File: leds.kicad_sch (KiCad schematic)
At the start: 22 parts, among them U2 AMS1117-5.0

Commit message: before auto route
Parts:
- removed D43: WS2812B-2020, LED_SMD:LED_WS2812B_PLCC4_5.0x5.0mm_P3.2mm, symbol LED:WS2812B-2020
- added C14, C15: 1uF, Capacitor_SMD:C_0402_1005Metric, symbol Device:C
- added Q1: BSS138, Package_TO_SOT_SMD:SOT-23, symbol Transistor_FET:BSS138
- added R5, R6: 10K, Resistor_SMD:R_0201_0603Metric, symbol Device:R
- renumbered D25 to D24, D27 to D25, D29 to D26, D31 to D27, D32 to D28, D30 to D29, D28 to D30, D26 to D31, D24 to D32, D35 to D34, D37 to D35, D39 to D36, D41 to D37, D42 to D38, D40 to D39, D38 to D40, D36 to D41, D34 to D42
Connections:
- net GND: now also C14.2, C15.2
- net LED_5V: now also C15.1, R6.1
- net LED_PIN: now also Q1.2 (S), R5.2; no longer D23.3 (DIN)
- net nRF_VDDH renamed 3.2V-5V
- net 3.2V-5V: now also C14.1
- new net DATA: D23.3 (DIN), Q1.3 (D), R6.2
- new net V_SYS: Q1.1 (G), R5.1
- no-connect marks 1 -> 0
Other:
- note removed: "LEDs"
- moved on the sheet: D23, D24, D25, D26, D27, D28, D29, D30, D31, D32, D33, D34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

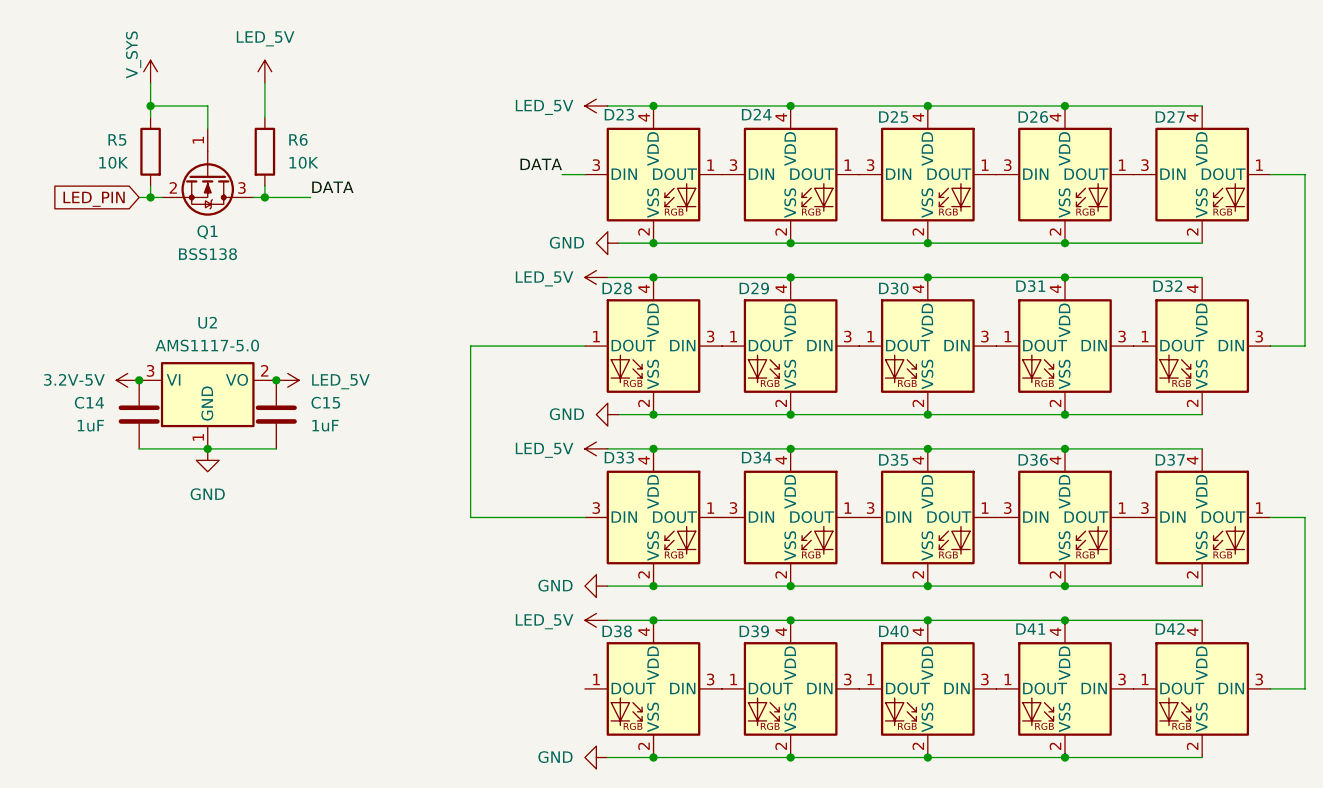
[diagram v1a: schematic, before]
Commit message: reassigned basic components, now comes the leds
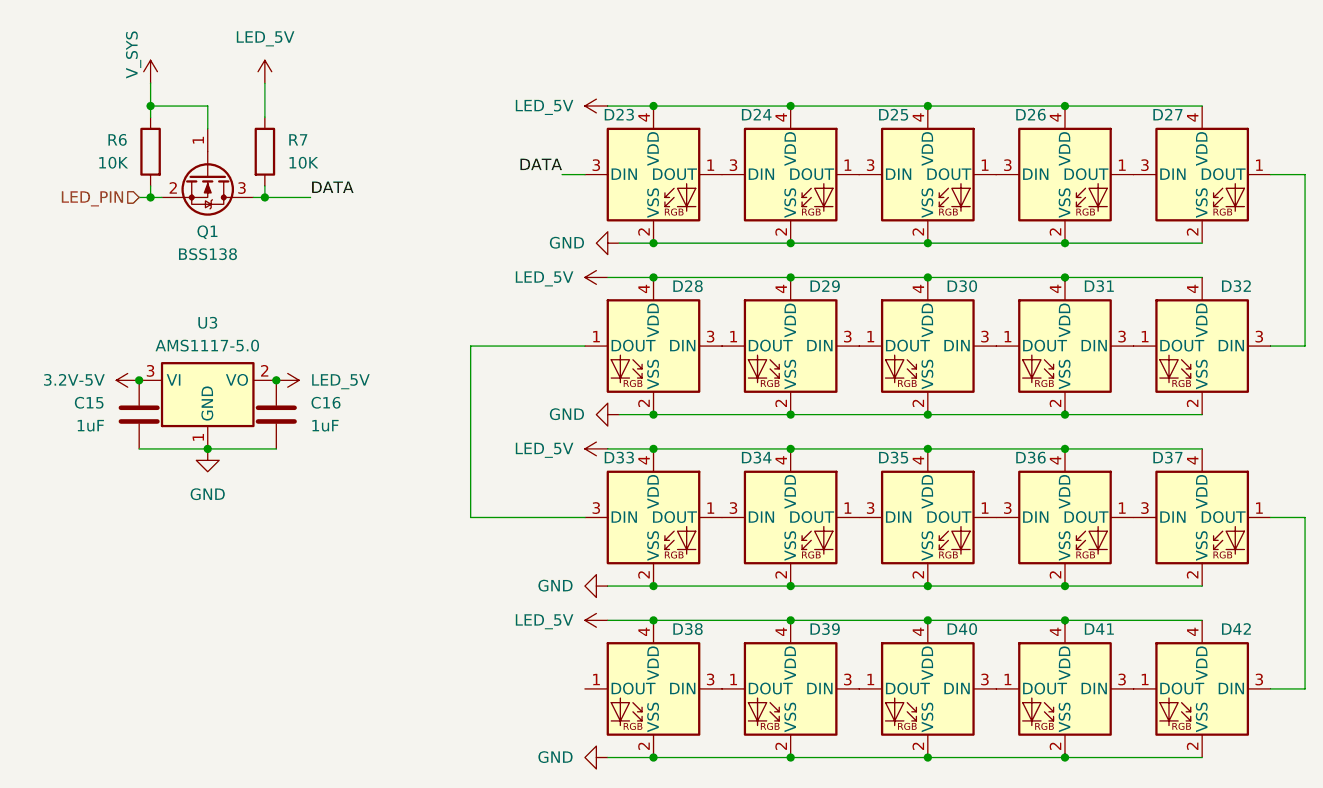
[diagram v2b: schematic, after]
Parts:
- removed D23, D24, D25, D26, D27, D28, D29, D30, D31, D32, D33, D34, D35, D36, D37, D38, D39, D40, D41, D42: WS2812B-2020, LED_SMD:LED_WS2812B_PLCC4_5.0x5.0mm_P3.2mm, symbol LED:WS2812B-2020
- added D23, D24, D25, D26, D27, D28, D29, D30, D31, D32, D33, D34, D35, D36, D37, D38, D39, D40, D41, D42: SK6812MINI, Keebio_Parts:SK6812-MINI-E, symbol LED:SK6812MINI
- renumbered C14 to C15, C15 to C16, R5 to R6, R6 to R7, U2 to U3
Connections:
- net DATA: now also D23.3 (DIN)
- net GND: now also D23.2 (VSS), D24.2 (VSS), D25.2 (VSS), D26.2 (VSS), D27.2 (VSS), D28.2 (VSS), D29.2 (VSS), D30.2 (VSS), D31.2 (VSS), D32.2 (VSS), D33.2 (VSS), D34.2 (VSS), D35.2 (VSS), D36.2 (VSS), D37.2 (VSS), D38.2 (VSS), D39.2 (VSS), D40.2 (VSS), D41.2 (VSS), D42.2 (VSS)
- net LED_5V: now also D23.4 (VDD), D24.4 (VDD), D25.4 (VDD), D26.4 (VDD), D27.4 (VDD), D28.4 (VDD), D29.4 (VDD), D30.4 (VDD), D31.4 (VDD), D32.4 (VDD), D33.4 (VDD), D34.4 (VDD), D35.4 (VDD), D36.4 (VDD), D37.4 (VDD), D38.4 (VDD), D39.4 (VDD), D40.4 (VDD), D41.4 (VDD), D42.4 (VDD)
- new net: D39.3 (DIN), D40.1 (DOUT)
- new net: D40.3 (DIN), D41.1 (DOUT)
- new net: D26.1 (DOUT), D27.3 (DIN)
- new net: D25.1 (DOUT), D26.3 (DIN)
- new net: D28.3 (DIN), D29.1 (DOUT)
- new net: D29.3 (DIN), D30.1 (DOUT)
- new net: D23.1 (DOUT), D24.3 (DIN)
- new net: D24.1 (DOUT), D25.3 (DIN)
- new net: D35.1 (DOUT), D36.3 (DIN)
- new net: D34.1 (DOUT), D35.3 (DIN)
- new net: D41.3 (DIN), D42.1 (DOUT)
- new net: D33.1 (DOUT), D34.3 (DIN)
- new net: D30.3 (DIN), D31.1 (DOUT)
- new net: D31.3 (DIN), D32.1 (DOUT)
- new net: D37.1 (DOUT), D42.3 (DIN)
- new net: D36.1 (DOUT), D37.3 (DIN)
- new net: D38.3 (DIN), D39.1 (DOUT)
- new net: D27.1 (DOUT), D32.3 (DIN)
- new net: D28.1 (DOUT), D33.3 (DIN)

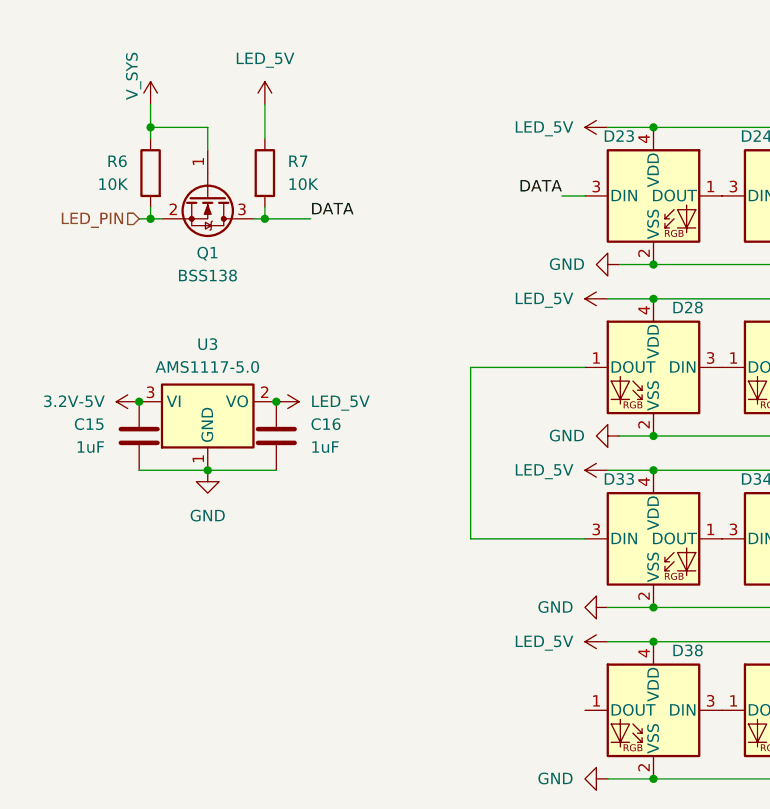
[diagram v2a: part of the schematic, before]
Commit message: placed right side
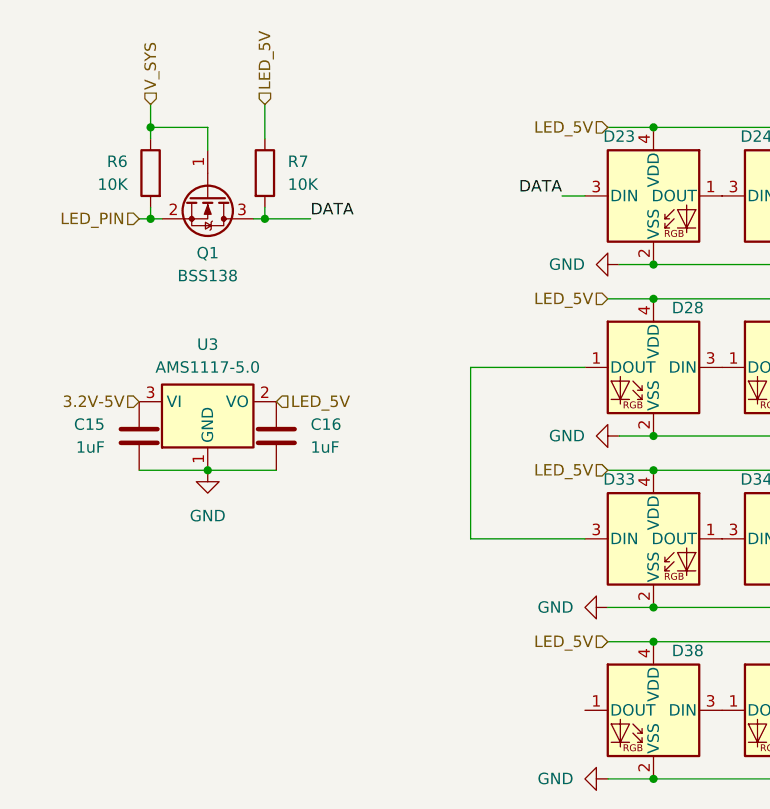
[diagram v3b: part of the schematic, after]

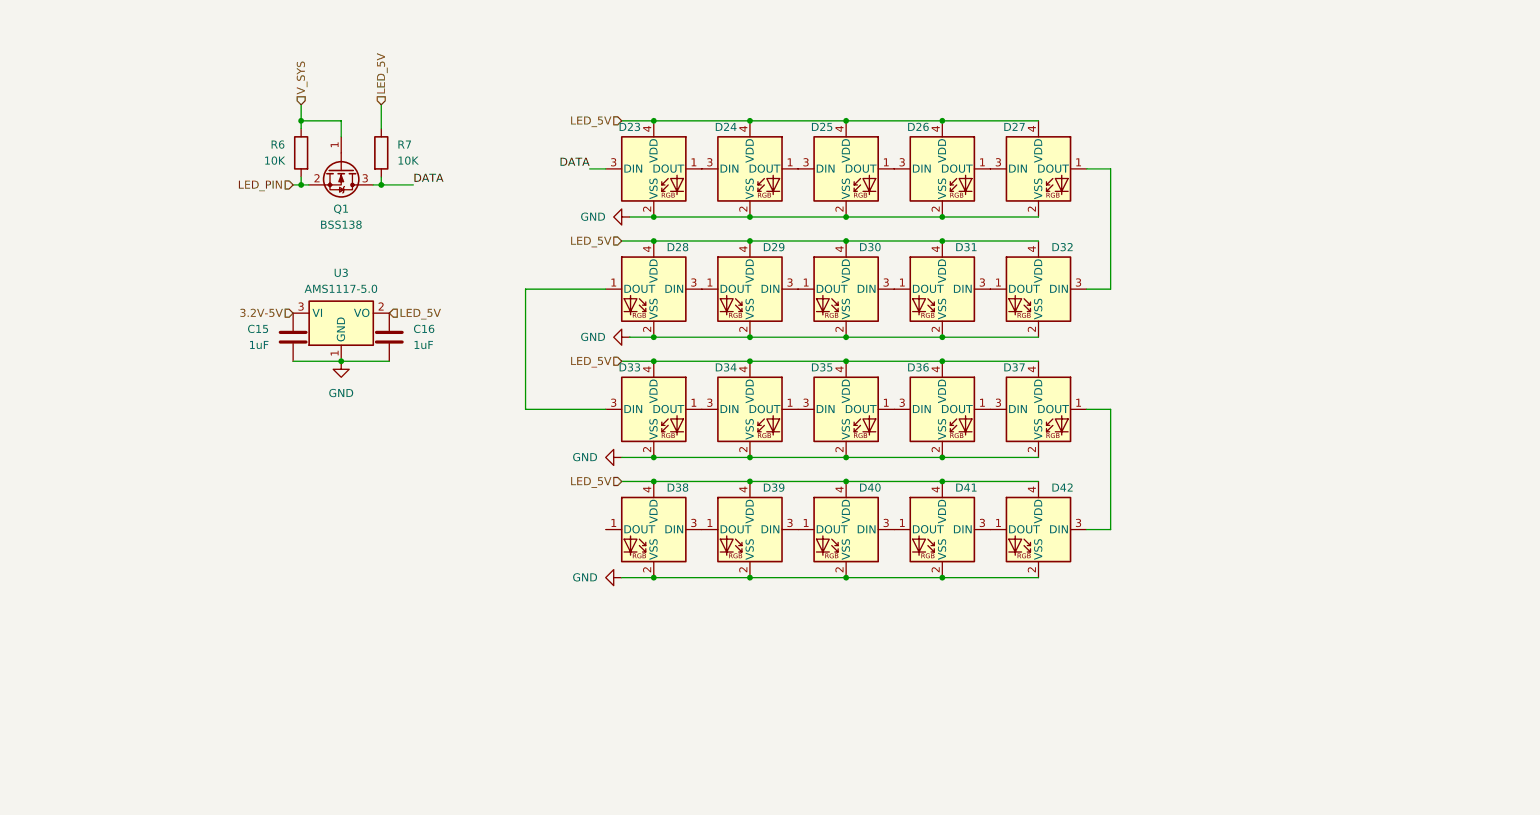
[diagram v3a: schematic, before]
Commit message: wired up the new votlage converter, removed small smd componenets
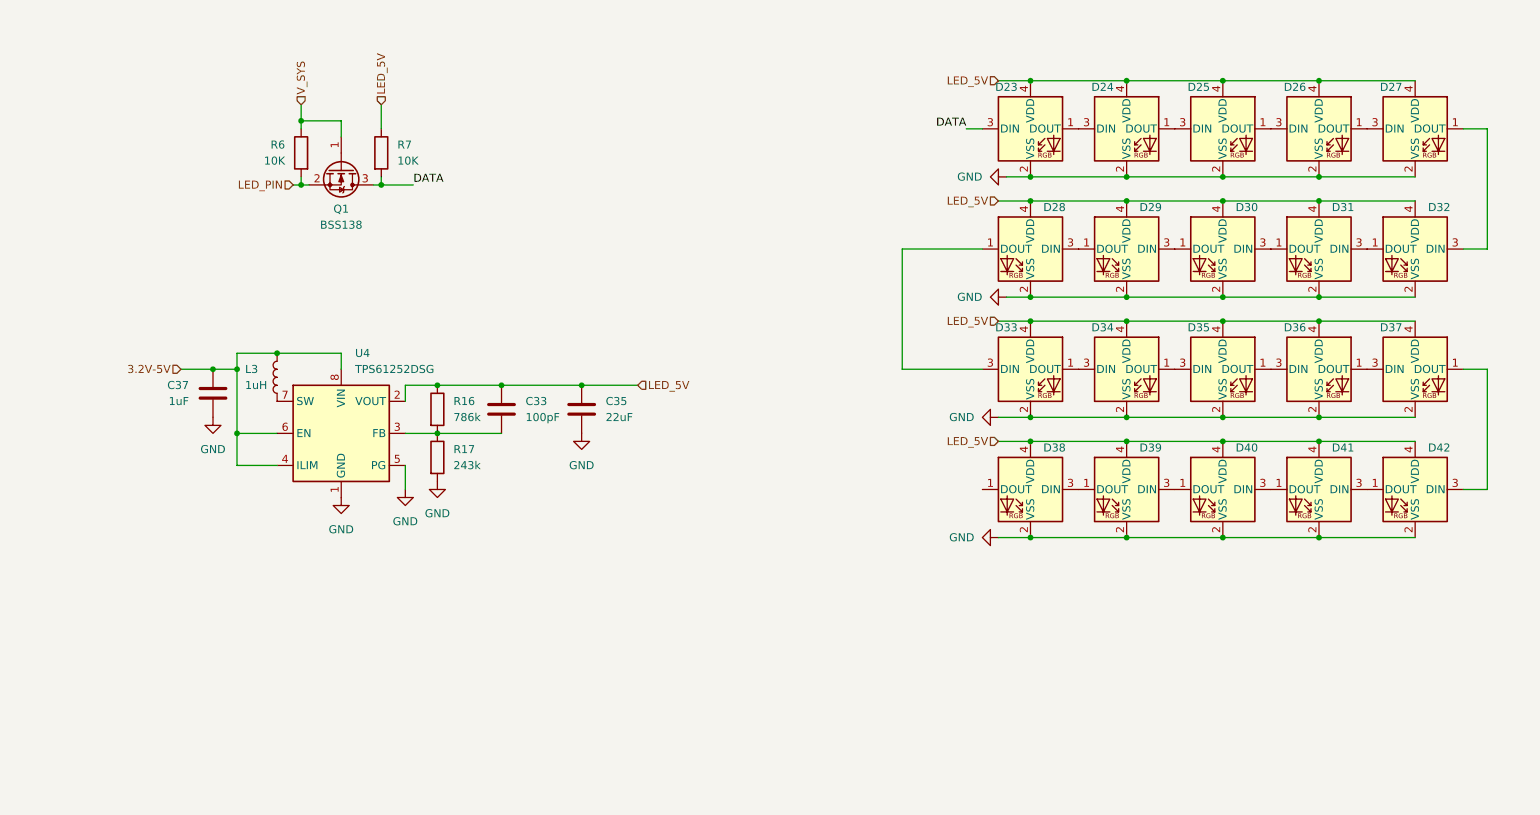
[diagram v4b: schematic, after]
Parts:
- removed C15, C16: 1uF, Capacitor_SMD:C_0402_1005Metric, symbol Device:C
- removed U3: AMS1117-5.0, Package_TO_SOT_SMD:SOT-223-3_TabPin2, symbol Regulator_Linear:AMS1117-5.0
- added C33: 100pF, Capacitor_SMD:C_0603_1608Metric, symbol Device:C
- added C35: 22uF, Capacitor_SMD:C_0603_1608Metric, symbol Device:C
- added C37: 1uF, Capacitor_SMD:C_0603_1608Metric, symbol Device:C
- added L3: 1uH, Inductor_SMD:L_0402_1005Metric, symbol Device:L
- added R16: 786k, Resistor_SMD:R_0402_1005Metric, symbol Device:R
- added R17: 243k, Resistor_SMD:R_0402_1005Metric, symbol Device:R
- added U4: TPS61252DSG, Package_SON:WSON-8-1EP_2x2mm_P0.5mm_EP0.9x1.6mm, symbol Regulator_Switching:TPS61252DSG
- R6, R7: footprint Resistor_SMD:R_0201_0603Metric -> Resistor_SMD:R_0402_1005Metric
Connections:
- net 3.2V-5V: now also C37.1, L3.2, U4.4 (ILIM), U4.6 (EN), U4.8 (VIN)
- net GND: now also C35.2, C37.2, R17.2, U4.1 (GND), U4.5 (PG), U4.9 (GND)
- net LED_5V: now also C33.1, C35.1, R16.1, U4.2 (VOUT)
- new net: C33.2, R16.2, R17.1, U4.3 (FB)
- new net: L3.1, U4.7 (SW)
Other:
- moved on the sheet: D23, D24, D25, D26, D27, D28, D29, D30, D31, D32, D33, D34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

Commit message: placed components
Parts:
- C33, C35, C37: footprint Capacitor_SMD:C_0603_1608Metric -> Capacitor_SMD:C_0805_2012Metric
- renumbered R16 to R15
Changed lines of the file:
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@@
+		)
+	)
+	(label "LED_5V"
+		(at 96.52 72.39 0)
+		(fields_autoplaced yes)
+		(effects
+			(font
+				(size 1.27 1.27)
+			)
+			(justify left bottom)
 		)
 	)
@@
 			)
 		)
-		(property "Footprint" "Capacitor_SMD:C_0603_1608Metric"
+		(property "Footprint" "Capacitor_SMD:C_0805_2012Metric"
 			(at 49.8348 77.47 0)
 			(effects
@@
 			)
 		)
-		(property "Footprint" "Capacitor_SMD:C_0603_1608Metric"
+		(property "Footprint" "Capacitor_SMD:C_0805_2012Metric"
 			(at 110.1852 80.01 0)
 			(effects
@@
 			)
 		)
-		(property "Footprint" "Capacitor_SMD:C_0603_1608Metric"
+		(property "Footprint" "Capacitor_SMD:C_0805_2012Metric"
 			(at 97.4852 80.01 0)
 			(effects
@@
 		(dnp no)
 		(fields_autoplaced yes)
-		(property "Reference" "R16"
+		(property "Reference" "R15"
 			(at 88.9 74.9299 0)
 			(effects

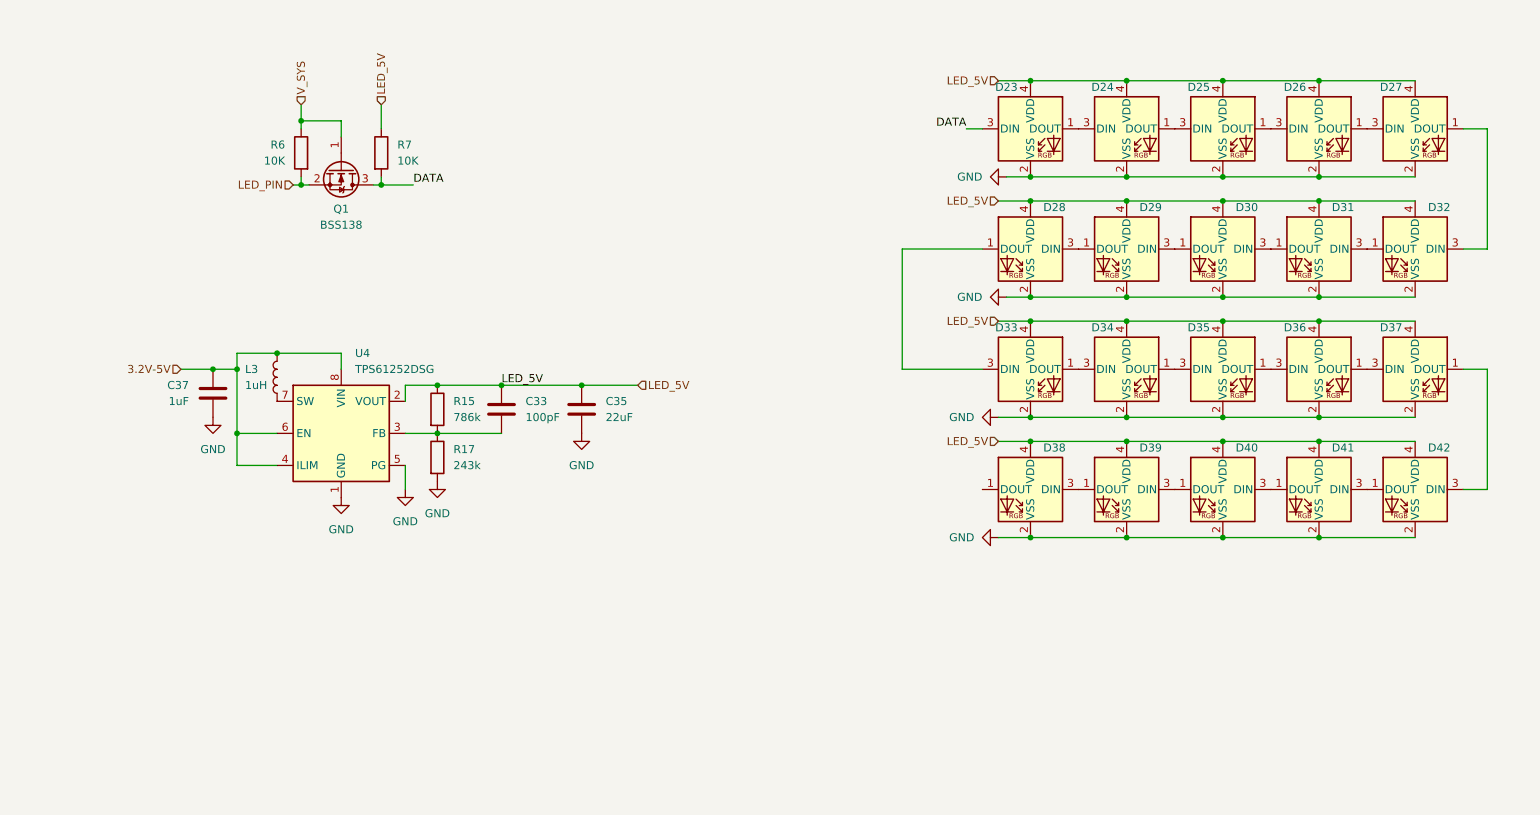
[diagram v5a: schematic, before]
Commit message: adding power and battery management
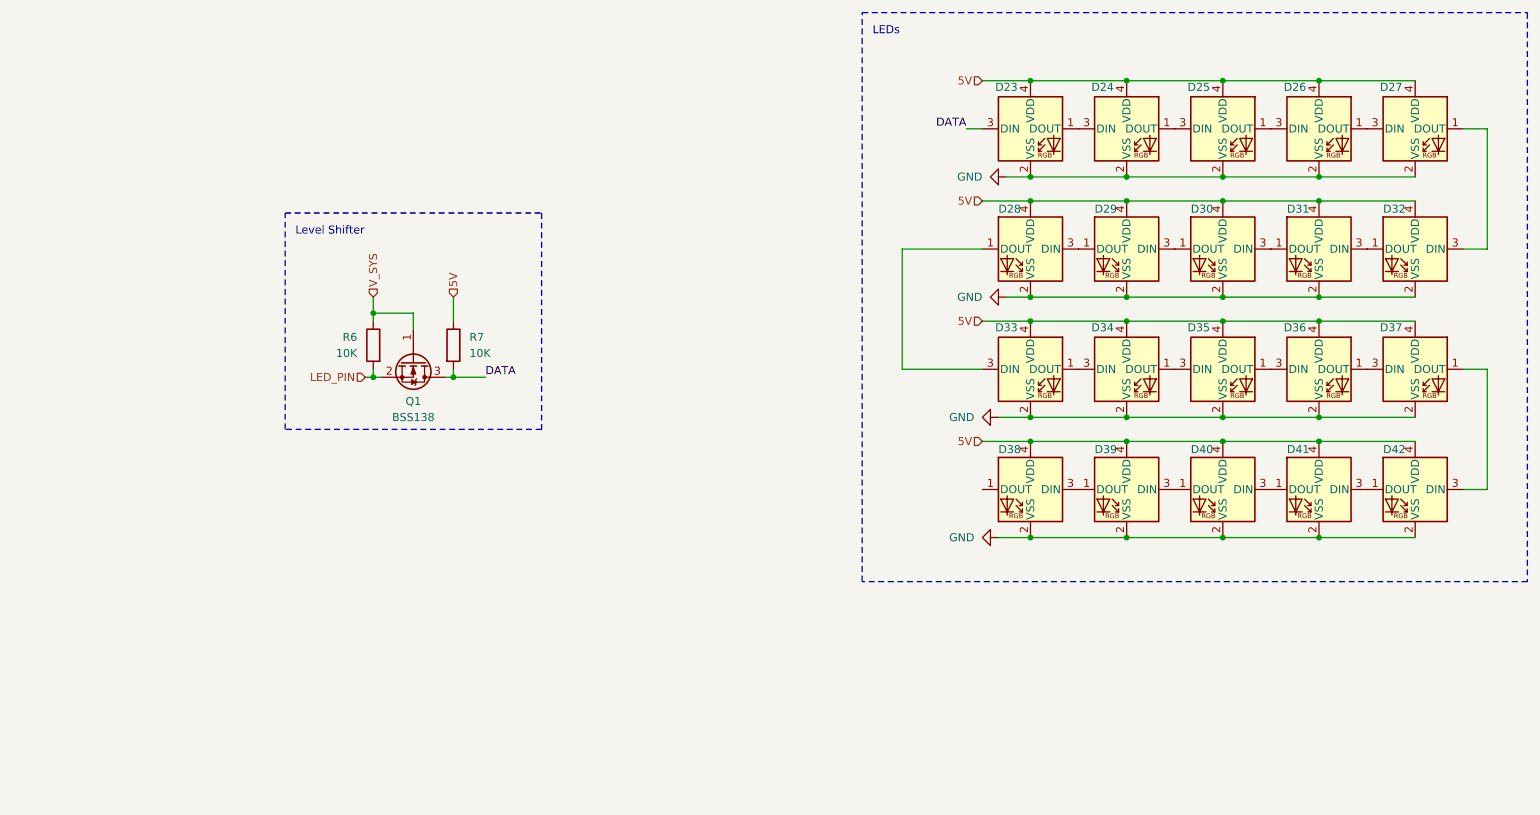
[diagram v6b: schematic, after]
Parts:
- removed C33: 100pF, Capacitor_SMD:C_0805_2012Metric, symbol Device:C
- removed C35: 22uF, Capacitor_SMD:C_0805_2012Metric, symbol Device:C
- removed C37: 1uF, Capacitor_SMD:C_0805_2012Metric, symbol Device:C
- removed L3: 1uH, Inductor_SMD:L_0402_1005Metric, symbol Device:L
- removed R15: 786k, Resistor_SMD:R_0402_1005Metric, symbol Device:R
- removed R17: 243k, Resistor_SMD:R_0402_1005Metric, symbol Device:R
- removed U4: TPS61252DSG, Package_SON:WSON-8-1EP_2x2mm_P0.5mm_EP0.9x1.6mm, symbol Regulator_Switching:TPS61252DSG
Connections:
- net LED_5V renamed 5V
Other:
- note added: "LEDs"
- note added: "Level Shifter"
- moved on the sheet: Q1, R6, R7
